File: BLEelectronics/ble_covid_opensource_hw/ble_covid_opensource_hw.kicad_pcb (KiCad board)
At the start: 2 copper layers, 40.7 x 31.3 mm, 35 parts, among them IC1 LTC4412xS6, IC2 PCF8523T, IC3 MX25R6435FM2IL0, IC4 LTC4054LES5-4.2#TRPBF, J1 Nordic_nRF52840_breakout, J4 Conn_01x01_Female, Q1 Si2307CDS, Q2 Si7463DP, U1 LP5907MFX-3.3, U2 BAT-HLD-001, U3 ESD401, U4 ESD401

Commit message: Schematic draft, working on Antenna layout.
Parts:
- added C1: , CAPC0603X03L_C, F.Cu at (122.7, 36.6)
- added C10: Not mounted, CAPC0603X03L_C, F.Cu at (124.7, 34.4)
- added C10: 1pF, Capacitor_SMD:C_0603_1608Metric, F.Cu at (135.6, 47.4)
- added C11: , CAPC0603X03L_C, F.Cu at (124.7, 35.0)
- added C11: 4.7uF, Capacitor_SMD:C_0603_1608Metric, F.Cu at (139.6, 44.9)
- added C12: , CAPC0603X03L_C, F.Cu at (126.9, 36.3)
- added C12: 1.5pF, Capacitor_SMD:C_0603_1608Metric, F.Cu at (130.9, 56.1)
- added C13: 100nF, Capacitor_SMD:C_0603_1608Metric, F.Cu at (135.6, 49.9)
- added C14: 0, Capacitor_SMD:C_0603_1608Metric, F.Cu at (135.0, 53.5)
- added C15: 100pF, Capacitor_SMD:C_0603_1608Metric, F.Cu at (139.6, 47.4)
- added C16: 0, Capacitor_SMD:C_0603_1608Metric, F.Cu at (143.6, 44.9)
- added C17: 820pF, Capacitor_SMD:C_0603_1608Metric, F.Cu at (135.0, 56.1)
- added C18: 4.7uF, Capacitor_SMD:C_0603_1608Metric, F.Cu at (126.9, 53.5)
- added C19: 1uF, Capacitor_SMD:C_0603_1608Metric, F.Cu at (139.6, 49.9)
- added C2: , CAPC0603X03L_C, F.Cu at (125.9, 36.5)
- added C20: 1uF, Capacitor_SMD:C_0603_1608Metric, F.Cu at (143.6, 47.4)
- added C21: 12pF, Capacitor_SMD:C_0603_1608Metric, F.Cu at (147.6, 44.9)
- added C22: 12pF, Capacitor_SMD:C_0603_1608Metric, F.Cu at (139.0, 54.9)
- added C25: Not mounted, CAPC0603X03L_C, F.Cu at (119.6, 36.8)
- added C26: , CAPC0603X03L_C, F.Cu at (117.8, 36.8)
- added C3: , CAPC0603X03L_C, F.Cu at (124.9, 33.5)
- added C4: , CAPC0603X03L_C, F.Cu at (123.3, 33.6)
- added C6: 1pF, Capacitor_SMD:C_0603_1608Metric, F.Cu at (139.0, 52.4)
- added C7: 0, Capacitor_SMD:C_0603_1608Metric, F.Cu at (135.6, 44.9)
- added C8: 12pF, Capacitor_SMD:C_0603_1608Metric, F.Cu at (126.9, 56.1)
- added C9: 12pF, Capacitor_SMD:C_0603_1608Metric, F.Cu at (130.9, 53.5)
- added J2: USB_B_Micro, Connector_USB:USB_Micro-B_Molex-105017-0001, F.Cu at (114.2, 46.6)
- added L1: , INDC0603X03L_C, F.Cu at (124.1, 33.0)
- added L1: L, Inductor_SMD:L_0402_1005Metric, F.Cu at (147.1, 49.6)
- added L2: 10uH, Inductor_SMD:L_0603_1608Metric, F.Cu at (143.6, 49.9)
- added L3: 15nH, Inductor_SMD:L_0402_1005Metric, F.Cu at (146.4, 52.1)
- added L4: 10uH, Inductor_SMD:L_0603_1608Metric, F.Cu at (143.0, 52.4)
- added R1: , RESC0603X03L_C, F.Cu at (118.7, 37.1)
- added R10: 0, Resistor_SMD:R_0603_1608Metric, F.Cu at (147.6, 47.4)
- added U1: Multi-protocol Bluetooth Low Energy, IEEE 802.15.4, ANT and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, AQFN50P700X700X85_HS-74N, F.Cu at (129.5, 32.2)
- added U5: TPD2E2U06, Package_TO_SOT_SMD:SOT-543, F.Cu at (111.0, 52.3)
- added U6: nRF52840, Package_DFN_QFN:Nordic_AQFN-73-1EP_7x7mm_P0.5mm, F.Cu at (129.3, 48.0)
- added X1: , BT-XTAL_2016, F.Cu at (124.3, 36.6)
- added Y1: 32MHz, Crystal:Crystal_SMD_2016-4Pin_2.0x1.6mm, F.Cu at (142.9, 55.5)
- J1: value Nordic_nRF52840_breakout -> USB_A_PLUG; footprint 0my_footprints:Nordic_nRF52840_FeatherHeader -> 0my_footprints:usbA-PCB
- moved J1 33.3 mm to (102.6, 56.2)
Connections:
- J1 pad 1: /CS -> /5Vusb
- J1 pad 2: /SO -> /D-
- J1 pad 3: /SCLK -> /D+
- J1 pad 4: /WP -> GND
- U2 pad 1: /3V -> Net-(U2-Pad1)
- U2 pad 3: /3V -> Net-(U2-Pad1)
- U3 pad 2: /3V -> Net-(U2-Pad1)
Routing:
- net (no net): track 0.00 -> 53.2 mm

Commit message: Partial progress on hw mvp 1b.
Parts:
- removed the C1 at (122.7, 36.6)
- removed the C10 at (124.7, 34.4)
- removed the C11 at (124.7, 35.0)
- removed the C12 at (126.9, 36.3)
- removed the C2 at (125.9, 36.5)
- removed C25: Not mounted, CAPC0603X03L_C
- removed C26: , CAPC0603X03L_C
- removed the C3 at (124.9, 33.5)
- removed the C4 at (123.3, 33.6)
- removed J1: USB_A_PLUG, 0my_footprints:usbA-PCB
- removed JP1, JP2, JP4: Jumper_2_Open, Jumper:SolderJumper-2_P1.3mm_Open_RoundedPad1.0x1.5mm
- removed the L1 at (124.1, 33.0)
- removed Q2: Si7463DP, Package_SO:PowerPAK_SO-8_Single
- removed the R1 at (118.7, 37.1)
- removed R2, R3: 0, Resistor_SMD:R_0603_1608Metric_Pad1.05x0.95mm_HandSolder
- removed the U1 at (129.5, 32.2)
- removed X1: , BT-XTAL_2016
- added C23: 4.7uF, Capacitor_SMD:C_0603_1608Metric_Pad1.05x0.95mm_HandSolder, F.Cu at (138.0, 81.1)
- R8, R9: value 4.7K -> 10K
- U5: footprint Package_TO_SOT_SMD:SOT-543 -> Package_TO_SOT_SMD:SOT-553
- moved U5 36.7 mm to (135.1, 80.0)
- moved J2 36.4 mm to (135.1, 76.4), turned to 180 degrees
- moved FID2 28.8 mm to (125.5, 102.7)
- moved IC3 18.8 mm to (115.9, 87.9)
- moved IC2 17.8 mm to (114.0, 99.5)
- moved J4 17.8 mm to (112.6, 94.0)
- moved R8 17.8 mm to (117.1, 93.1)
- moved R9 17.8 mm to (116.2, 94.7)
- moved U6 16.4 mm to (124.0, 63.5)
- moved C5 5.31 mm to (140.5, 82.0)
- moved D3 5.31 mm to (142.5, 82.0)
- moved U4 4.78 mm to (137.9, 79.7), turned to 0 degrees
- moved C4 4.68 mm to (141.8, 74.7)
- moved U1 4.31 mm to (141.9, 77.6)
- moved R5 2.84 mm to (145.5, 76.2), turned to 90 degrees
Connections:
- net Net-(U6-PadL1) renamed /nRF52840_QIAA_R/LED1
- net Net-(U6-PadN1) renamed /nRF52840_QIAA_R/LED2_R
- net Net-(U6-PadR1) renamed /nRF52840_QIAA_R/LED2_G
- net Net-(U6-PadR24) renamed /nRF52840_QIAA_R/SW1
- net Net-(U6-PadU1) renamed /nRF52840_QIAA_R/LED2_B
- D3 pad 1: Net-(D3-Pad1) -> /VDD_3V
- J2 pad 1: Net-(J2-Pad1) -> /5Vusb
- J2 pad 2: Net-(J2-Pad2) -> /D-
- J2 pad 3: Net-(J2-Pad3) -> /D+
- J2 pad 5: Net-(J2-Pad5) -> GND
- J2 pad 6: Net-(J2-Pad6) -> GND
- JP3 pad 2: Net-(JP3-Pad2) -> /VDD_3V
- Q1 pad 2: Net-(JP3-Pad2) -> /VDD_3V
- U5 pad 3: /D- -> /D+
- U6 pad A14: /nRF52840_QIAA_R/RESET -> Net-(U6-PadA14)
- U6 pad AC15: /nRF52840_QIAA_R/RESET -> /nRF52840_QIAA_R/SCLK
- U6 pad AC17: /nRF52840_QIAA_R/RESET -> /nRF52840_QIAA_R/SO
- U6 pad AC19: /nRF52840_QIAA_R/RESET -> /nRF52840_QIAA_R/SIO3
- U6 pad AC21: /nRF52840_QIAA_R/RESET -> Net-(U6-PadAC21)
- U6 pad AD10: /nRF52840_QIAA_R/SO -> /nRF52840_QIAA_R/SCL
- U6 pad AD12: /nRF52840_QIAA_R/SCLK -> /nRF52840_QIAA_R/CS
- U6 pad AD16: /nRF52840_QIAA_R/WP -> /nRF52840_QIAA_R/SI
- U6 pad AD18: /nRF52840_QIAA_R/SI -> /nRF52840_QIAA_R/WP
- U6 pad AD22: /nRF52840_QIAA_R/SCL -> Net-(U6-PadAD22)
- U6 pad AD8: /nRF52840_QIAA_R/CS -> Net-(U6-PadAD8)
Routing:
- net /VDD_3V: track 38.2 -> 23.8 mm, vias 2 -> 0
- net /SCLK: track 14.3 -> 0.00 mm
- net /SI: track 12.0 -> 0.00 mm
- net /CS: track 10.5 -> 0.00 mm
- net /RESET: track 10.3 -> 0.00 mm
- net Net-(JP1-Pad1): track 9.93 -> 0.00 mm
- net /SO: track 9.72 -> 0.00 mm
- net Net-(IC1-Pad5): track 19.0 -> 9.97 mm
- net /SDA: track 12.0 -> 4.08 mm
- net /SCL: track 10.5 -> 2.67 mm
- net Net-(JP4-Pad1): track 7.13 -> 0.00 mm
- net Net-(JP3-Pad2): track 6.13 -> 0.00 mm
- net Net-(JP2-Pad2): track 5.39 -> 0.00 mm
- net /WP: track 5.12 -> 0.00 mm
- net /D+: track 0.00 -> 3.29 mm
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
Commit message: MVP 1b schematic almost ready for review.
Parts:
- moved IC3 66.1 mm to (181.8, 92.7)
- moved J4 66.1 mm to (178.6, 98.8)
- moved R8 66.1 mm to (183.0, 97.9)
- moved R9 66.1 mm to (182.1, 99.5)
- moved IC2 66.1 mm to (179.9, 104.4)
- moved U6 36.8 mm to (143.9, 94.4), turned to 180 degrees
- moved FID2 28.5 mm to (125.7, 74.2)
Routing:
- net (no net): track 53.2 -> 40.9 mm
- net Net-(C8-Pad2): track 0.00 -> 4.01 mm
- net Net-(C15-Pad1): track 0.00 -> 2.12 mm
- net Net-(C9-Pad2): track 0.00 -> 1.72 mm
- net /nRF52840_QIAA_R/VDD_3V: track 0.00 -> 1.71 mm
- net Net-(C16-Pad1): track 0.00 -> 1.46 mm

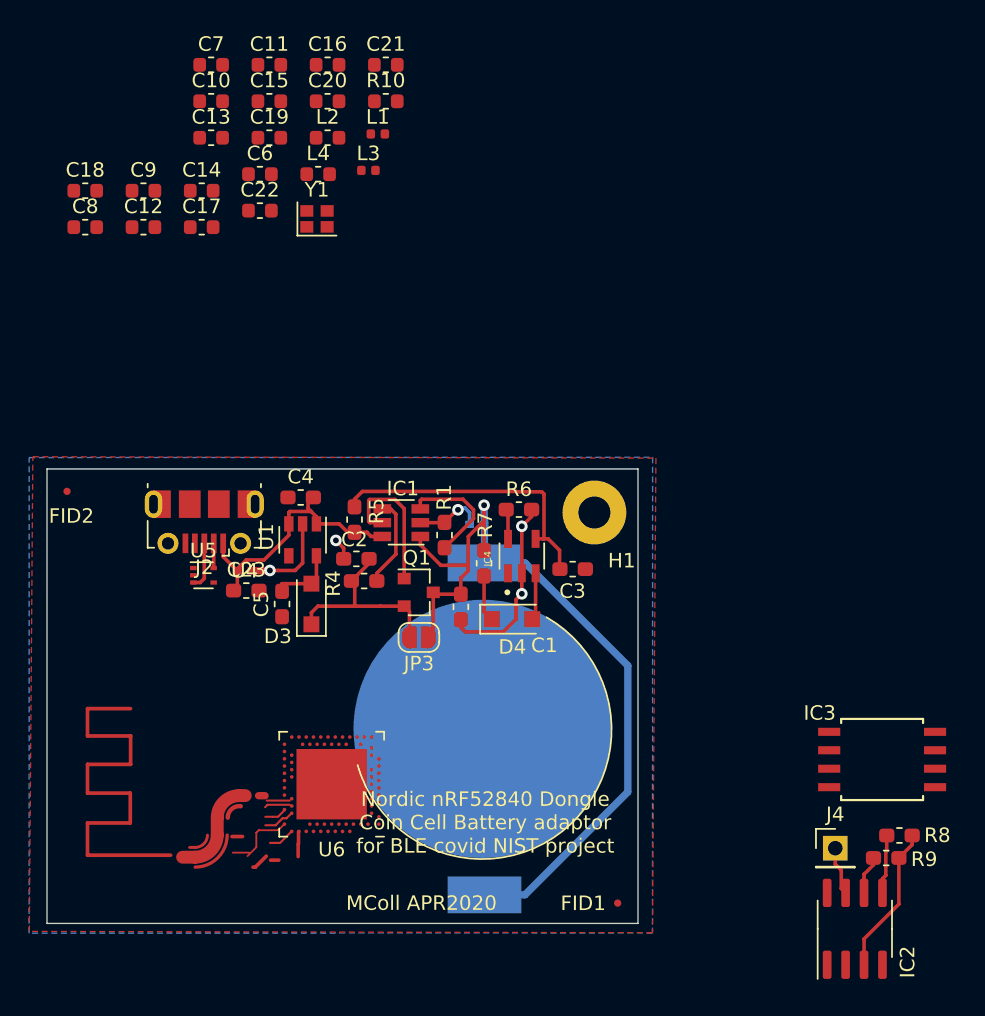
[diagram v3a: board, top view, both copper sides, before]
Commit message: hw mvp 1b schematic full draft ready for review
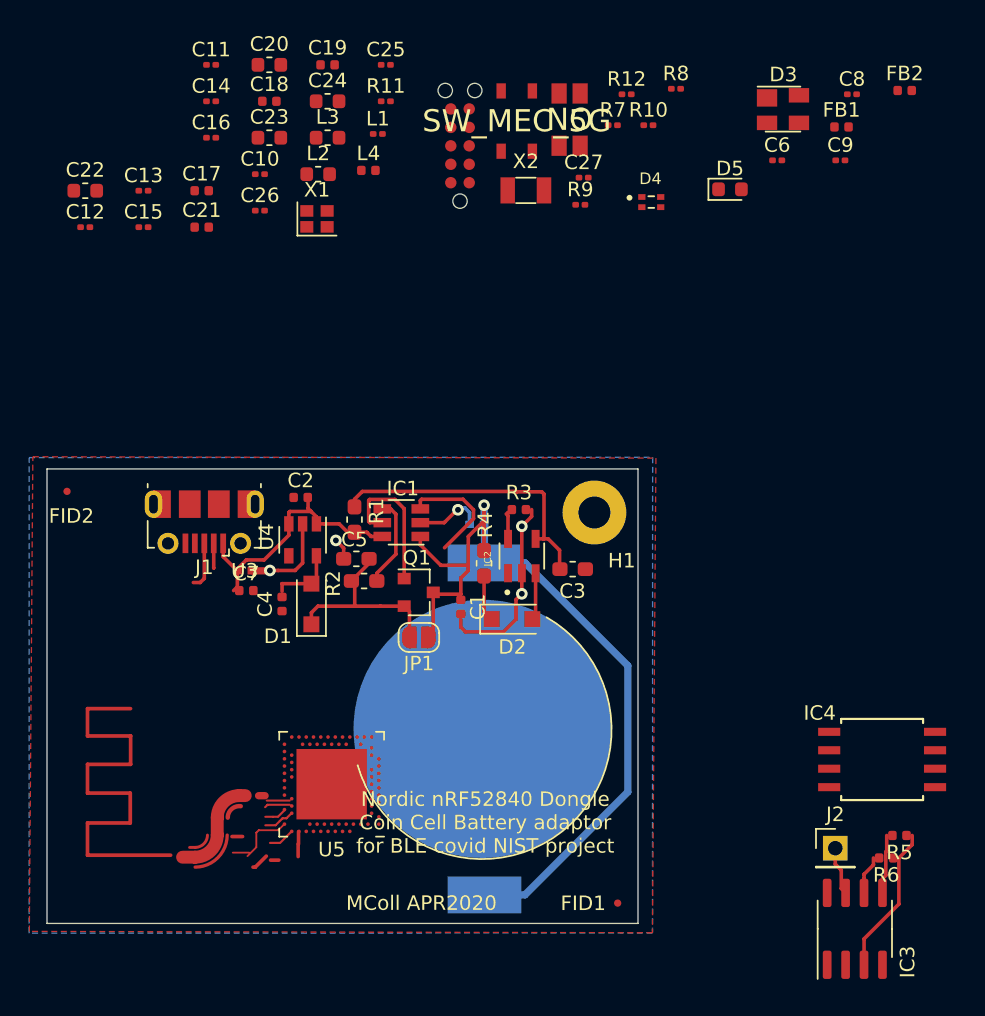
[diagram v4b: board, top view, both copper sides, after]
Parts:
- removed the R1 at (151.7, 77.3)
- removed the U5 at (135.1, 80.0)
- added C27: 100nF, Capacitor_SMD:C_0201_0603Metric, F.Cu at (161.3, 52.6)
- added C6: 0.01uF, Capacitor_SMD:C_0201_0603Metric, F.Cu at (174.6, 51.4)
- added C8: 0.1uF, Capacitor_SMD:C_0201_0603Metric, F.Cu at (179.7, 46.9)
- added C9: 0.1uF, Capacitor_SMD:C_0201_0603Metric, F.Cu at (178.9, 51.4)
- added D3: PRTR5V0U2X, Package_TO_SOT_SMD:SOT-143, F.Cu at (175.0, 47.9)
- added D4: LED_ABRG, 0my_footprints:LED_APHF1608SEEQBDZGKC, F.Cu at (165.9, 54.3)
- added D5: LED, LED_SMD:LED_0603_1608Metric, F.Cu at (171.3, 53.4)
- added FB1: Ferrite_Bead, Inductor_SMD:L_0402_1005Metric, F.Cu at (179.0, 49.1)
- added FB2: Ferrite_Bead, Inductor_SMD:L_0402_1005Metric, F.Cu at (183.4, 46.6)
- added J3: Conn_02x05_Odd_Even, 0my_footprints:TC2050-IDC-NLFP, F.Cu at (152.7, 50.4)
- added R10: 390, Resistor_SMD:R_0201_0603Metric, F.Cu at (165.7, 49.0)
- added R12: 10K, Resistor_SMD:R_0201_0603Metric, F.Cu at (164.2, 46.9)
- added R7: 220, Resistor_SMD:R_0201_0603Metric, F.Cu at (163.3, 49.0)
- added R8: 1k2, Resistor_SMD:R_0201_0603Metric, F.Cu at (167.6, 46.5)
- added R9: 2k2, Resistor_SMD:R_0201_0603Metric, F.Cu at (161.0, 54.5)
- added SW1: NO, 0my_footprints:EVQP7A_J_B_K, F.Cu at (160.3, 48.6)
- added SW2: SW_MEC_5G, 0my_footprints:C&K_PTS810, F.Cu at (156.7, 48.7)
- added X2: 32.768KHZ, Crystal:Crystal_SMD_3215-2Pin_3.2x1.5mm, F.Cu at (157.3, 53.5)
- C1: footprint Capacitor_SMD:C_0603_1608Metric_Pad1.05x0.95mm_HandSolder -> Capacitor_SMD:C_0402_1005Metric
- C10: renamed from C6; footprint Capacitor_SMD:C_0603_1608Metric -> Capacitor_SMD:C_0201_0603Metric
- C11: renamed from C7; value 0 -> N.C.; footprint Capacitor_SMD:C_0603_1608Metric -> Capacitor_SMD:C_0201_0603Metric
- C12: renamed from C8; footprint Capacitor_SMD:C_0603_1608Metric -> Capacitor_SMD:C_0201_0603Metric
- C13: renamed from C9; footprint Capacitor_SMD:C_0603_1608Metric -> Capacitor_SMD:C_0201_0603Metric
- C14: renamed from C10; footprint Capacitor_SMD:C_0603_1608Metric -> Capacitor_SMD:C_0201_0603Metric
- C15: renamed from C12; footprint Capacitor_SMD:C_0603_1608Metric -> Capacitor_SMD:C_0201_0603Metric
- C16: renamed from C13; footprint Capacitor_SMD:C_0603_1608Metric -> Capacitor_SMD:C_0201_0603Metric
- C17: renamed from C14; value 0 -> N.C.; footprint Capacitor_SMD:C_0603_1608Metric -> Capacitor_SMD:C_0402_1005Metric
- C18: renamed from C15; footprint Capacitor_SMD:C_0603_1608Metric -> Capacitor_SMD:C_0402_1005Metric
- C19: renamed from C16; value 0 -> N.C.; footprint Capacitor_SMD:C_0603_1608Metric -> Capacitor_SMD:C_0402_1005Metric
- C2: renamed from C4; footprint Capacitor_SMD:C_0603_1608Metric_Pad1.05x0.95mm_HandSolder -> Capacitor_SMD:C_0402_1005Metric
- C21: renamed from C17; footprint Capacitor_SMD:C_0603_1608Metric -> Capacitor_SMD:C_0402_1005Metric
- C25: renamed from C21; footprint Capacitor_SMD:C_0603_1608Metric -> Capacitor_SMD:C_0201_0603Metric
- C26: renamed from C22; footprint Capacitor_SMD:C_0603_1608Metric -> Capacitor_SMD:C_0201_0603Metric
- C4: renamed from C5; footprint Capacitor_SMD:C_0603_1608Metric_Pad1.05x0.95mm_HandSolder -> Capacitor_SMD:C_0402_1005Metric
- C7: renamed from C23; footprint Capacitor_SMD:C_0603_1608Metric_Pad1.05x0.95mm_HandSolder -> Capacitor_SMD:C_0402_1005Metric
- L1: value L -> 3.9nH; footprint Inductor_SMD:L_0402_1005Metric -> Inductor_SMD:L_0201_0603Metric
- R11: renamed from R10; footprint Resistor_SMD:R_0603_1608Metric -> Resistor_SMD:R_0201_0603Metric
- R3: renamed from R6; footprint Resistor_SMD:R_0603_1608Metric_Pad1.05x0.95mm_HandSolder -> Resistor_SMD:R_0402_1005Metric
- R5: renamed from R8; footprint Resistor_SMD:R_0603_1608Metric_Pad1.05x0.95mm_HandSolder -> Resistor_SMD:R_0402_1005Metric
- R6: renamed from R9; footprint Resistor_SMD:R_0603_1608Metric_Pad1.05x0.95mm_HandSolder -> Resistor_SMD:R_0402_1005Metric
- renumbered C11 to C20, C18 to C22, C19 to C23, C20 to C24, C2 to C5, D3 to D1, D4 to D2, IC4 to IC2, IC2 to IC3, IC3 to IC4, J2 to J1, J4 to J2, JP3 to JP1, L4 to L2, L2 to L3, L3 to L4, R5 to R1, R4 to R2, R7 to R4, U2 to U1, U3 to U2, U4 to U3, U1 to U4, U6 to U5, Y1 to X1
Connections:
- net Net-(AE1-Pad1) renamed /nRF52840_QIAA_R/ANTENNA
- C22 pad 1: /nRF52840_QIAA_R/VDD_3V -> /VDD_3V
- C23 pad 1: /nRF52840_QIAA_R/VDD_3V -> /VDD_3V
- C7 pad 1: /5Vusb -> Net-(C6-Pad2)
- IC1 pad 3: Net-(IC1-Pad3) -> GND
- J1 pad 1: /5Vusb -> Net-(C6-Pad2)
- J1 pad 5: GND -> Net-(FB1-Pad2)
- L2 pad 1: /nRF52840_QIAA_R/VDD_3V -> /VDD_3V
- U5 pad A22: /nRF52840_QIAA_R/VDD_3V -> /VDD_3V
- U5 pad AA24: Net-(U6-PadAA24) -> /nRF52840_QIAA_R/SWDCLK
- U5 pad AC15: /nRF52840_QIAA_R/SCLK -> /SCLK
- U5 pad AC17: /nRF52840_QIAA_R/SO -> /SO
- U5 pad AC19: /nRF52840_QIAA_R/SIO3 -> /RESET
- U5 pad AC24: Net-(U6-PadAC24) -> /nRF52840_QIAA_R/SWDIO
- U5 pad AD10: /nRF52840_QIAA_R/SCL -> /SCL
- U5 pad AD12: /nRF52840_QIAA_R/CS -> /CS
- U5 pad AD14: /nRF52840_QIAA_R/VDD_3V -> /VDD_3V
- U5 pad AD16: /nRF52840_QIAA_R/SI -> /SI
- U5 pad AD18: /nRF52840_QIAA_R/WP -> /WP
- U5 pad AD20: /nRF52840_QIAA_R/SDA -> /SDA
- U5 pad AD23: /nRF52840_QIAA_R/VDD_3V -> /VDD_3V
- U5 pad B1: /nRF52840_QIAA_R/VDD_3V -> /VDD_3V
- U5 pad W1: /nRF52840_QIAA_R/VDD_3V -> /VDD_3V
- U5 pad Y2: Net-(U6-PadY2) -> /VDD_3V
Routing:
- net Net-(IC1-Pad3): track 8.02 -> 0.00 mm
- net GND: track 25.4 -> 33.5 mm
- net /nRF52840_QIAA_R/VDD_3V: track 1.71 -> 0.00 mm
- net /VDD_3V: track 23.8 -> 25.6 mm

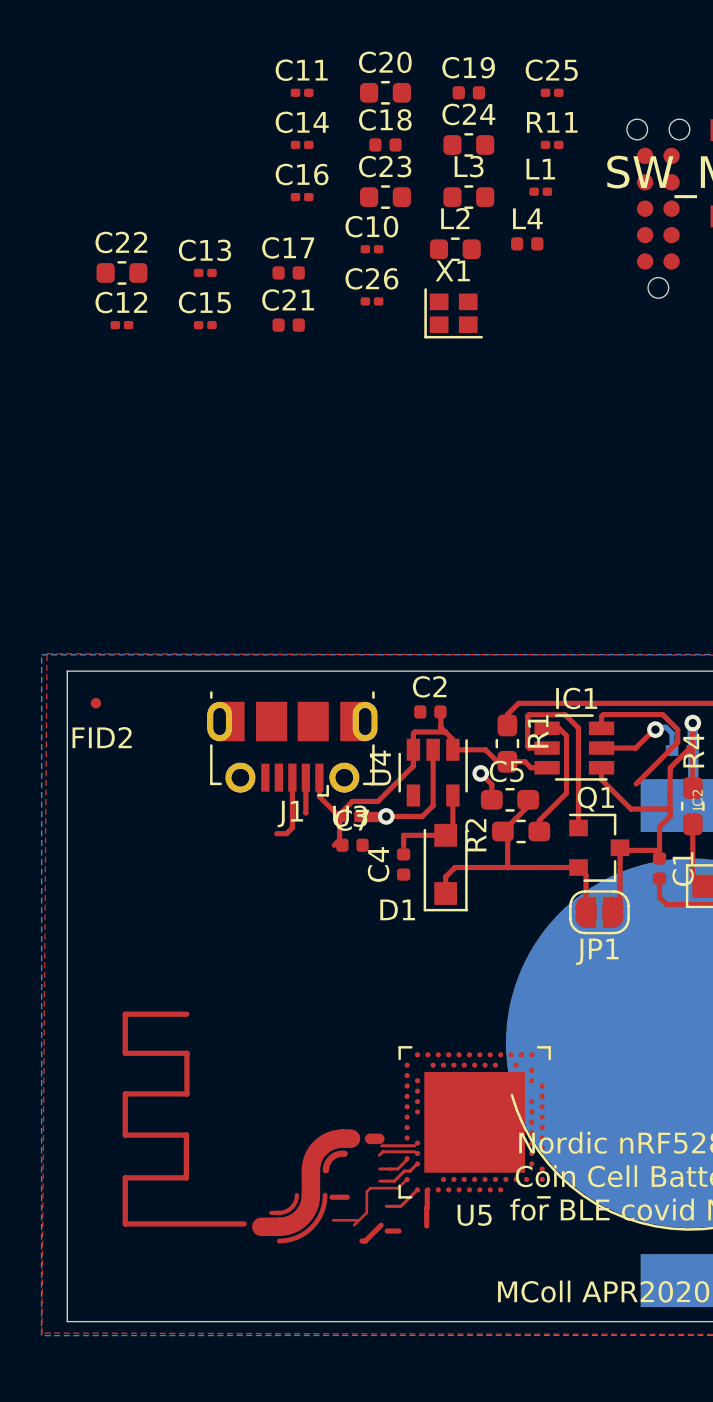
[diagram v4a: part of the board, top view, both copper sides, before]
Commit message: Antenna layout implemented
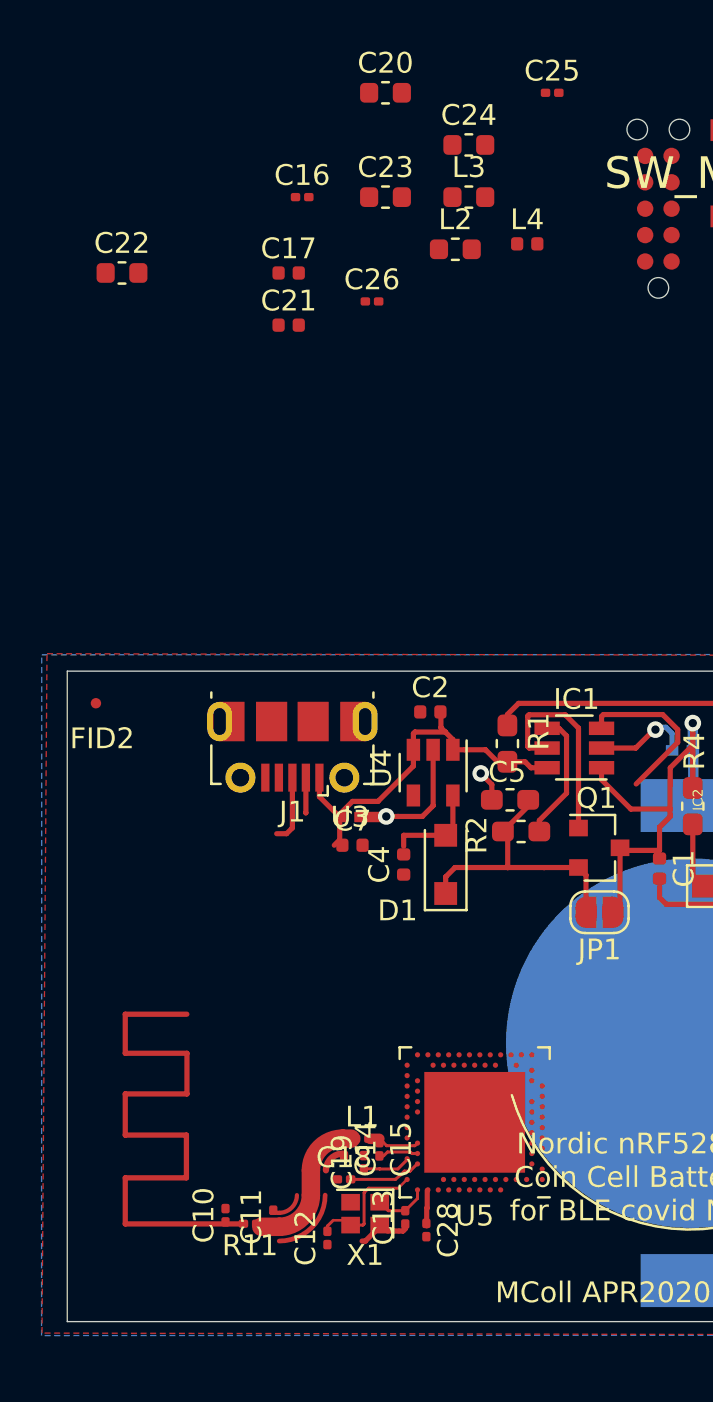
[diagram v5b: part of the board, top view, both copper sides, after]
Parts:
- added C28: 100nF, Capacitor_SMD:C_0201_0603Metric, F.Cu at (141.6, 99.6)
- C18, C19: footprint Capacitor_SMD:C_0402_1005Metric -> Capacitor_SMD:C_0201_0603Metric
- moved C11 54.1 mm to (134.2, 99.0), turned to 90 degrees
- moved R11 53.9 mm to (133.1, 99.3), turned to 180 degrees
- moved C19 51.7 mm to (138.6, 96.3), turned to 90 degrees
- moved C18 49.8 mm to (137.6, 97.2)
- moved C14 48.4 mm to (137.6, 95.7), turned to 270 degrees
- moved C10 47.0 mm to (131.9, 98.9), turned to 90 degrees
- moved C13 46.5 mm to (140.6, 99.0), turned to 90 degrees
- moved L1 46.4 mm to (138.5, 95.2)
- moved C12 45.0 mm to (136.8, 100.0), turned to 90 degrees
- moved X1 43.5 mm to (138.6, 98.8), turned to 180 degrees
- moved C15 40.5 mm to (139.3, 95.7), turned to 270 degrees
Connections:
- C18 pad 1: Net-(C18-Pad1) -> GND
- C18 pad 2: GND -> Net-(C18-Pad2)
- C19 pad 2: Net-(C18-Pad1) -> GND
- U5 pad A22: /VDD_3V -> Net-(C28-Pad1)
- U5 pad D23: Net-(C18-Pad1) -> Net-(C18-Pad2)
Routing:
- net (no net): track 40.9 -> 1.19 mm
- net /nRF52840_QIAA_R/ANTENNA: track 0.00 -> 30.6 mm
- net GND: track 33.5 -> 38.2 mm
- net Net-(C18-Pad2): track 0.00 -> 3.47 mm
- net Net-(C15-Pad1): track 0.00 -> 2.40 mm
- net Net-(C12-Pad2): track 4.01 -> 6.25 mm
- net Net-(C18-Pad1): track 2.12 -> 0.00 mm
- net Net-(C28-Pad1): track 0.00 -> 1.71 mm
- net /VDD_3V: track 25.6 -> 23.8 mm
- net Net-(C11-Pad1): track 0.00 -> 1.27 mm
- net Net-(C13-Pad2): track 1.72 -> 2.65 mm
- net Net-(C19-Pad1): track 1.46 -> 2.23 mm
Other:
- net class Default: clearance 0.2 -> 0.127
- rule pad_to_mask_clearance: 0.051 -> 0
- rule trace_clearance: 0.2 -> 0.127
- rule trace_min: 0.2 -> 0.145
